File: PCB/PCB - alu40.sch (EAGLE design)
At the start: 163 parts, among them IC1 XB3303ASOT23, IC2 TP4054-42-SOT25-R, J1 SK-3296S-01-L1, J2 USB4510-03-1-A, Q2 PMOSFET, Q3 PMOSFET, Q5 PMOSFET, Q6 NMOSFET, U1 ISP1807-LRISP1807-LR_ISP1807-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, X1 BM02B-SRSS-TB

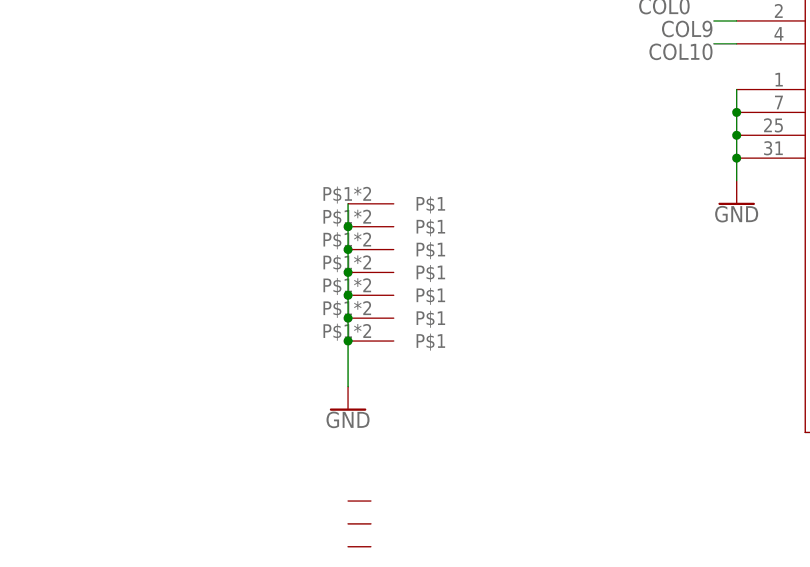
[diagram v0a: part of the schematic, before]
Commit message: Add standoffs
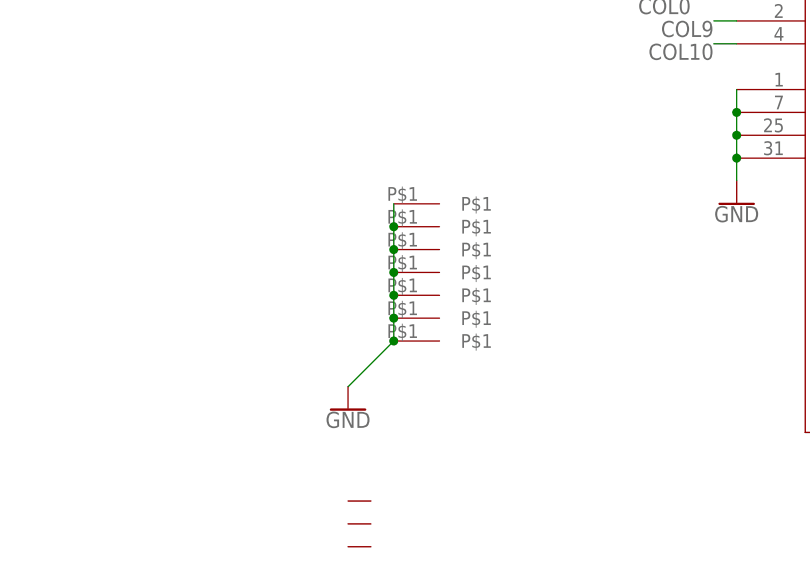
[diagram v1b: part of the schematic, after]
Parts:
- U$1, U$2, U$3, U$4, U$5, U$6, U$7: value 2.5MM_HOLE -> SINSOOM2; device Volume_V1:2.5MM_HOLE -> Volume_V1:SINSOOM2
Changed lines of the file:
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@@
 <part name="GND9" library="SparkFun-PowerSymbols" library_urn="urn:adsk.eagle:library:530" deviceset="GND" device=""/>
 <part name="GND71" library="SparkFun-PowerSymbols" library_urn="urn:adsk.eagle:library:530" deviceset="GND" device=""/>
-<part name="U$1" library="Volume_V1" library_urn="urn:adsk.eagle:library:32198814" deviceset="2.5MM_HOLE" device="" package3d_urn="urn:adsk.eagle:package:32198940/1"/>
-<part name="U$2" library="Volume_V1" library_urn="urn:adsk.eagle:library:32198814" deviceset="2.5MM_HOLE" device="" package3d_urn="urn:adsk.eagle:package:32198940/1"/>
-<part name="U$3" library="Volume_V1" library_urn="urn:adsk.eagle:library:32198814" deviceset="2.5MM_HOLE" device="" package3d_urn="urn:adsk.eagle:package:32198940/1"/>
-<part name="U$4" library="Volume_V1" library_urn="urn:adsk.eagle:library:32198814" deviceset="2.5MM_HOLE" device="" package3d_urn="urn:adsk.eagle:package:32198940/1"/>
-<part name="U$5" library="Volume_V1" library_urn="urn:adsk.eagle:library:32198814" deviceset="2.5MM_HOLE" device="" package3d_urn="urn:adsk.eagle:package:32198940/1"/>
-<part name="U$6" library="Volume_V1" library_urn="urn:adsk.eagle:library:32198814" deviceset="2.5MM_HOLE" device="" package3d_urn="urn:adsk.eagle:package:32198940/1"/>
-<part name="U$7" library="Volume_V1" library_urn="urn:adsk.eagle:library:32198814" deviceset="2.5MM_HOLE" device="" package3d_urn="urn:adsk.eagle:package:32198940/1"/>
+<part name="U$1" library="Volume_V1" library_urn="urn:adsk.eagle:library:32198814" deviceset="SINSOOM2" device="" package3d_urn="urn:adsk.eagle:package:37877257/4"/>
+<part name="U$2" library="Volume_V1" library_urn="urn:adsk.eagle:library:32198814" deviceset="SINSOOM2" device="" package3d_urn="urn:adsk.eagle:package:37877257/4"/>
+<part name="U$3" library="Volume_V1" library_urn="urn:adsk.eagle:library:32198814" deviceset="SINSOOM2" device="" package3d_urn="urn:adsk.eagle:package:37877257/4"/>
+<part name="U$4" library="Volume_V1" library_urn="urn:adsk.eagle:library:32198814" deviceset="SINSOOM2" device="" package3d_urn="urn:adsk.eagle:package:37877257/4"/>
+<part name="U$5" library="Volume_V1" library_urn="urn:adsk.eagle:library:32198814" deviceset="SINSOOM2" device="" package3d_urn="urn:adsk.eagle:package:37877257/4"/>
+<part name="U$6" library="Volume_V1" library_urn="urn:adsk.eagle:library:32198814" deviceset="SINSOOM2" device="" package3d_urn="urn:adsk.eagle:package:37877257/4"/>
+<part name="U$7" library="Volume_V1" library_urn="urn:adsk.eagle:library:32198814" deviceset="SINSOOM2" device="" package3d_urn="urn:adsk.eagle:package:37877257/4"/>
 <part name="GND3" library="SparkFun-PowerSymbols" library_urn="urn:adsk.eagle:library:530" deviceset="GND" device=""/>
 <part name="47" library="Volume_V1" library_urn="urn:adsk.eagle:library:32198814" deviceset="CHERRY" device="" package3d_urn="urn:adsk.eagle:package:32198958/1"/>
@@
 <segment>
 <pinref part="U$1" gate="G$1" pin="P$1"/>
-<wire x1="-261.62" y1="-43.18" x2="-261.62" y2="-45.72" width="0.1524" layer="91"/>
+<wire x1="-256.54" y1="-43.18" x2="-256.54" y2="-45.72" width="0.1524" layer="91"/>
 <pinref part="U$2" gate="G$1" pin="P$1"/>
-<wire x1="-261.62" y1="-45.72" x2="-261.62" y2="-48.26" width="0.1524" layer="91"/>
-<junction x="-261.62" y="-45.72"/>
+<wire x1="-256.54" y1="-45.72" x2="-256.54" y2="-48.26" width="0.1524" layer="91"/>
+<junction x="-256.54" y="-45.72"/>
 <pinref part="U$3" gate="G$1" pin="P$1"/>
-<wire x1="-261.62" y1="-48.26" x2="-261.62" y2="-50.8" width="0.1524" layer="91"/>
-<junction x="-261.62" y="-48.26"/>
+<wire x1="-256.54" y1="-48.26" x2="-256.54" y2="-50.8" width="0.1524" layer="91"/>
+<junction x="-256.54" y="-48.26"/>
 <pinref part="U$4" gate="G$1" pin="P$1"/>
-<wire x1="-261.62" y1="-50.8" x2="-261.62" y2="-53.34" width="0.1524" layer="91"/>
-<junction x="-261.62" y="-50.8"/>
+<wire x1="-256.54" y1="-50.8" x2="-256.54" y2="-53.34" width="0.1524" layer="91"/>
+<junction x="-256.54" y="-50.8"/>
 <pinref part="U$5" gate="G$1" pin="P$1"/>
-<wire x1="-261.62" y1="-53.34" x2="-261.62" y2="-55.88" width="0.1524" layer="91"/>
-<junction x="-261.62" y="-53.34"/>
+<wire x1="-256.54" y1="-53.34" x2="-256.54" y2="-55.88" width="0.1524" layer="91"/>
+<junction x="-256.54" y="-53.34"/>
 <pinref part="U$6" gate="G$1" pin="P$1"/>
-<wire x1="-261.62" y1="-55.88" x2="-261.62" y2="-58.42" width="0.1524" layer="91"/>
-<junction x="-261.62" y="-55.88"/>
+<wire x1="-256.54" y1="-55.88" x2="-256.54" y2="-58.42" width="0.1524" layer="91"/>
+<junction x="-256.54" y="-55.88"/>
 <pinref part="U$7" gate="G$1" pin="P$1"/>
-<wire x1="-261.62" y1="-58.42" x2="-261.62" y2="-63.5" width="0.1524" layer="91"/>
-<junction x="-261.62" y="-58.42"/>
+<wire x1="-256.54" y1="-58.42" x2="-261.62" y2="-63.5" width="0.1524" layer="91"/>
+<junction x="-256.54" y="-58.42"/>
 <pinref part="GND3" gate="1" pin="GND"/>
 </segment>
